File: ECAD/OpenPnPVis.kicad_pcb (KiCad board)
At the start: 4 copper layers, 40 x 47.4 mm, 73 parts, among them J1 USB3_B, J2 Conn_01x02, J3 Conn_01x02, Q1 CJ2305, U1 AMS1117-3.3, U10 AP2127K-2.5, U2 ﻿AR0144, U3 FT602Q, U4 AP2127K-2.8, U5 TPD4EUSB30, U6 AP2127K-1.2, U7 ATtiny10-TS, U8 74LVC2G74, U9 TPD2EUSB30, Y1 30MHz

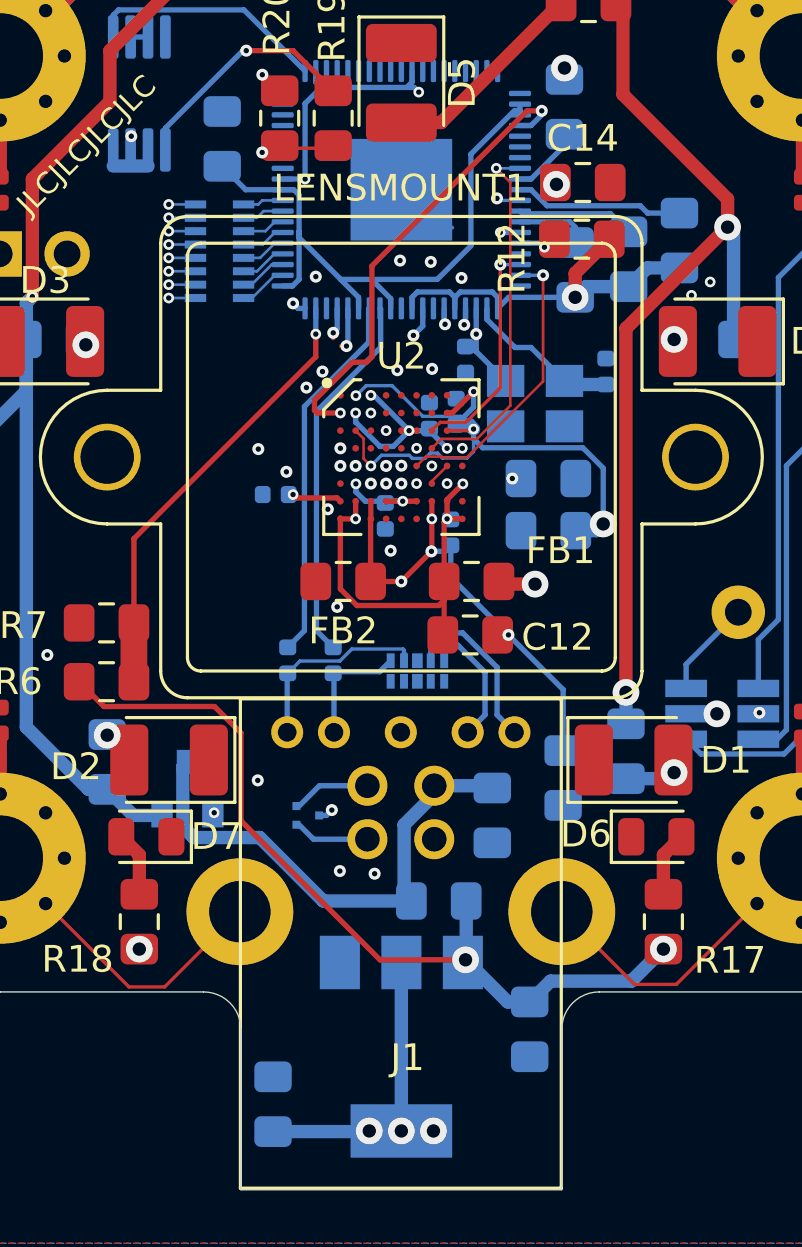
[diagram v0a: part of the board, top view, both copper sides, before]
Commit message: Added Courtyard to Lens mount
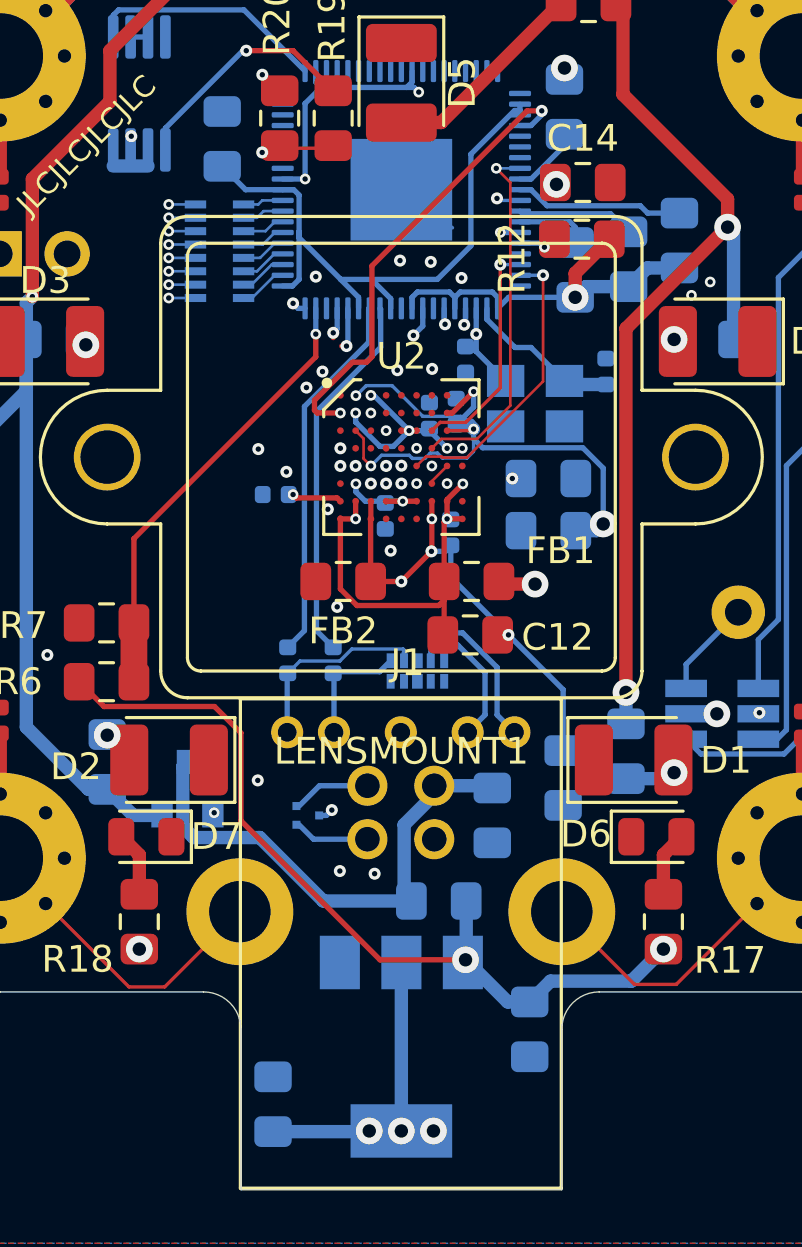
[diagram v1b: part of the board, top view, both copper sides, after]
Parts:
- J1: footprint Image_Sensors:U235-091N-4BLRC16-4-5 -> OpenPnPVis:U235-091N-4BLRC16-4-5
- LENSMOUNT1: footprint Image_Sensors:CMT168-1122F -> OpenPnPVis:CMT168-1122F
- U2: footprint Image_Sensors:BGA-72_9x8_5.565x5.545mm -> OpenPnPVis:BGA-72_9x8_5.565x5.545mm
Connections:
- U3 pad 77: GND -> (no net)

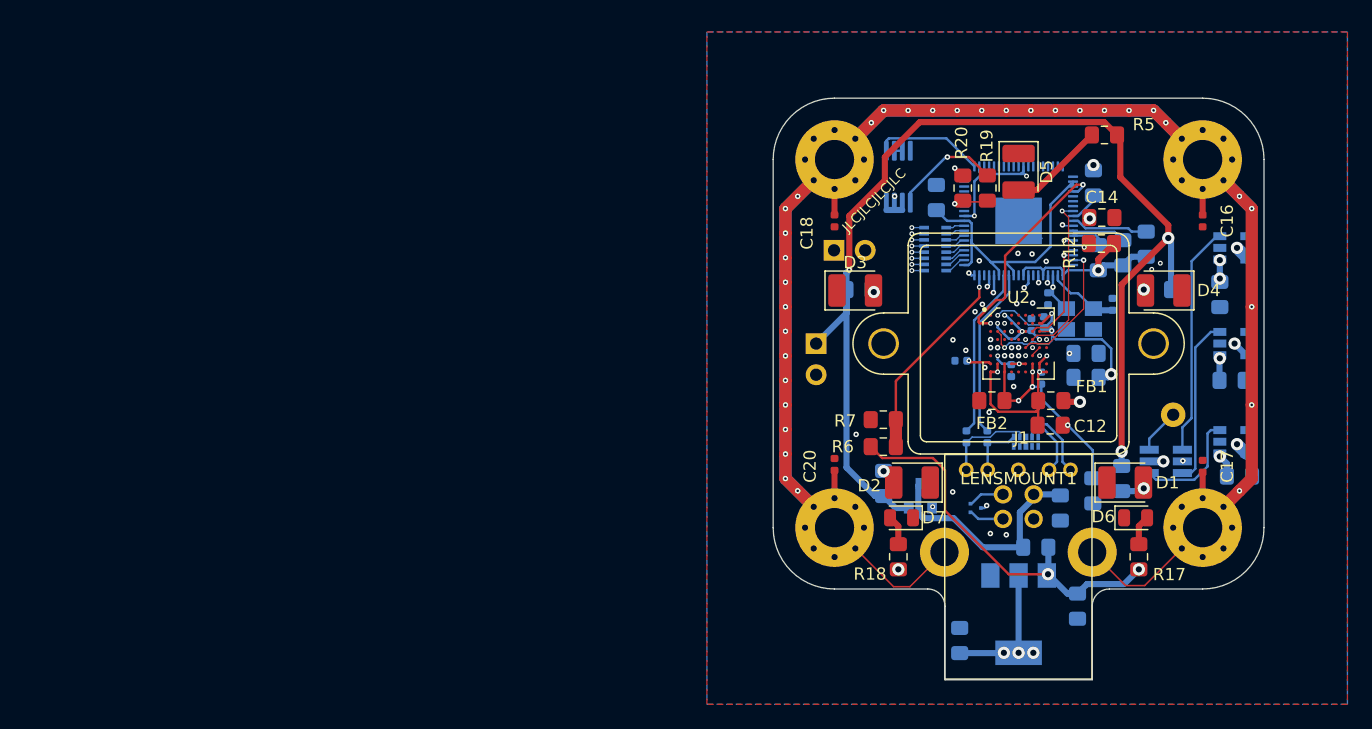
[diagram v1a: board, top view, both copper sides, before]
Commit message: Creation of Rev003
Creation of Rev003. This is a mini-sized board for easier fitment into tight spaces. The USB connector has changed to a USB Type-C. Some components have changed footprint to 0402.
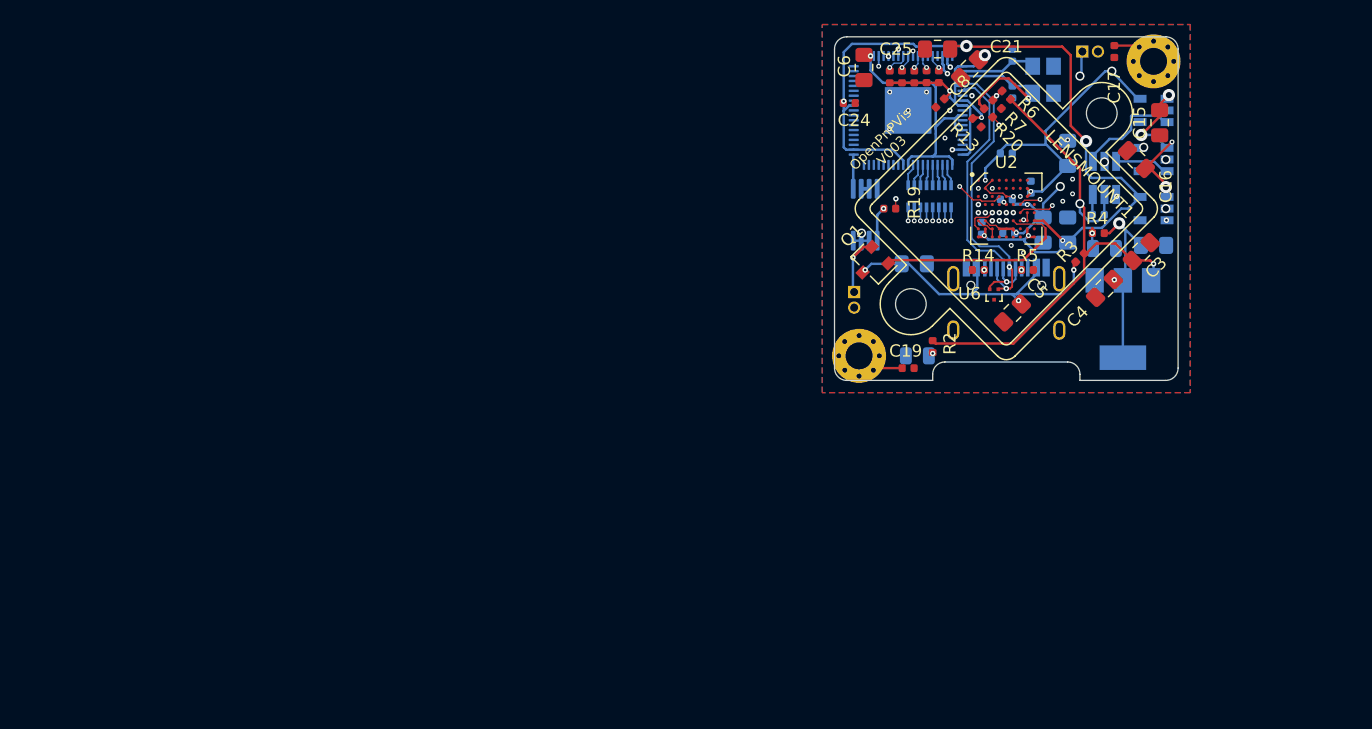
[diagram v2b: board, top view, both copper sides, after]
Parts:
- removed C20: 100nF, Capacitor_SMD:C_0402_1005Metric
- removed D3, D4, D5: LED, LED_SMD:LED_1210_3225Metric_Pad1.42x2.65mm_HandSolder
- removed D6, D7: LED, LED_SMD:LED_0805_2012Metric
- removed FB1, FB2: Ferrite_Bead_Small, Resistor_SMD:R_0805_2012Metric_Pad1.15x1.40mm_HandSolder
- removed H3, H4: M3, MountingHole:MountingHole_3.2mm_M3_Pad_Via
- removed J1: USB3_B, OpenPnPVis:U235-091N-4BLRC16-4-5
- removed R16: 0R, Resistor_SMD:R_0805_2012Metric_Pad1.15x1.40mm_HandSolder
- removed R17, R18: 100, Resistor_SMD:R_0805_2012Metric_Pad1.15x1.40mm_HandSolder
- removed TP1: TestPoint, TestPoint:TestPoint_Loop_D1.80mm_Drill1.0mm_Beaded
- removed U5: TPD4EUSB30, Package_SON:USON-10_2.5x1.0mm_P0.5mm
- added C24: 100nF, Capacitor_SMD:C_0402_1005Metric, F.Cu at (141.2, 85.4)
- added C25: 10uF, Capacitor_SMD:C_0805_2012Metric_Pad1.15x1.40mm_HandSolder, F.Cu at (148.4, 81.0)
- added J4: USB_C_Receptacle, Type-C:HRO-TYPE-C-31-M-12-Assembly, B.Cu at (154.0, 106.5)
- C1, C2: value 100nF -> 16pF
- C12, C14: moved to B.Cu
- C15, C21, C5: moved to F.Cu
- C16: value 100nF -> 10uF; footprint Capacitor_SMD:C_0402_1005Metric -> Capacitor_SMD:C_0805_2012Metric_Pad1.15x1.40mm_HandSolder
- C18: value 100nF -> 10uF; footprint Capacitor_SMD:C_0402_1005Metric -> Capacitor_SMD:C_0805_2012Metric_Pad1.15x1.40mm_HandSolder; moved to B.Cu
- C19, C8: value 10uF -> 100nF; footprint Capacitor_SMD:C_0805_2012Metric_Pad1.15x1.40mm_HandSolder -> Capacitor_SMD:C_0402_1005Metric; moved to F.Cu
- C3, C4: value 100nF -> 10uF; footprint Capacitor_SMD:C_0402_1005Metric -> Capacitor_SMD:C_0805_2012Metric_Pad1.15x1.40mm_HandSolder; moved to F.Cu
- C6: value 4.7uF -> 10uF; moved to F.Cu
- D1, D2: footprint LED_SMD:LED_1210_3225Metric_Pad1.42x2.65mm_HandSolder -> LED_SMD:LED_0805_2012Metric; moved to B.Cu
- H1, H2: footprint MountingHole:MountingHole_3.2mm_M3_Pad_Via -> MountingHole:MountingHole_2.2mm_M2_Pad_Via
- J2, J3: footprint Connector_PinHeader_2.54mm:PinHeader_1x02_P2.54mm_Vertical -> Connector_PinHeader_1.27mm:PinHeader_1x02_P1.27mm_Vertical
- Q1: value CJ2305 -> SMD-MOSFET-P-CH-8V-4.1A-CJ2305_SOT-23_; moved to F.Cu
- R1: value 100 -> 10K; footprint Resistor_SMD:R_0805_2012Metric_Pad1.15x1.40mm_HandSolder -> Resistor_SMD:R_0402_1005Metric
- R10, R11, R13, R8, R9: footprint Resistor_SMD:R_0805_2012Metric_Pad1.15x1.40mm_HandSolder -> Resistor_SMD:R_0402_1005Metric; moved to F.Cu
- R12, R19, R20, R6, R7: footprint Resistor_SMD:R_0805_2012Metric_Pad1.15x1.40mm_HandSolder -> Resistor_SMD:R_0402_1005Metric
- R14: value 0R -> 5.1K; footprint Resistor_SMD:R_0805_2012Metric_Pad1.15x1.40mm_HandSolder -> Resistor_SMD:R_0402_1005Metric; moved to F.Cu
- R2: value 100 -> 85; footprint Resistor_SMD:R_0805_2012Metric_Pad1.15x1.40mm_HandSolder -> Resistor_SMD:R_0402_1005Metric; moved to F.Cu
- R3, R4: value 100 -> 0R; footprint Resistor_SMD:R_0805_2012Metric_Pad1.15x1.40mm_HandSolder -> Resistor_SMD:R_0402_1005Metric; moved to F.Cu
- R5: value 100 -> 5.1K; footprint Resistor_SMD:R_0805_2012Metric_Pad1.15x1.40mm_HandSolder -> Resistor_SMD:R_0402_1005Metric
- U4: value AP2127K-2.8 -> ATtiny10-TS; footprint Package_TO_SOT_SMD:SOT-23-5 -> Package_TO_SOT_SMD:SOT-23-6_Handsoldering
- U6: value AP2127K-1.2 -> TPD2EUSB30; footprint Package_TO_SOT_SMD:SOT-23-5 -> Package_TO_SOT_SMD:Texas_DRT-3; moved to F.Cu
- U7: value ATtiny10-TS -> AP2127K-2.8; footprint Package_TO_SOT_SMD:SOT-23-6_Handsoldering -> Package_TO_SOT_SMD:SOT-23-5
- U9: value TPD2EUSB30 -> AP2127K-1.2; footprint Package_TO_SOT_SMD:Texas_DRT-3 -> Package_TO_SOT_SMD:SOT-23-5
- Y1: value 30MHz -> X3S030000BA1H-U
- moved H1 46.0 mm to (166.0, 82.0)
- moved C8 43.8 mm to (148.6, 85.4), turned to 225 degrees
- moved C17 34.6 mm to (162.8, 81.2), turned to 90 degrees
- moved C21 33.2 mm to (151.0, 82.6), turned to 225 degrees
- moved U9 31.9 mm to (166.0, 90.0), turned to 180 degrees
- moved H2 31.3 mm to (142.0, 106.0)
- moved C7 30.9 mm to (146.5, 98.5), turned to 180 degrees
- moved R6 30.4 mm to (154.0, 84.8), turned to 135 degrees
- moved U7 28.6 mm to (166.0, 86.0)
- moved C19 28.4 mm to (146.0, 107.0)
- moved R7 27.3 mm to (153.2, 85.5), turned to 135 degrees
- moved C18 26.1 mm to (166.0, 97.0), turned to 180 degrees
- moved J3 25.9 mm to (160.2, 81.2)
- moved U1 25.5 mm to (163.5, 103.0)
- moved D2 24.7 mm to (162.0, 97.2)
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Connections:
- net /FLASH_SIG renamed FLASH_SIG
- C11 pad 1: /VAA -> VAA
- C11 pad 2: GNDA -> GND
- C12 pad 1: /VAA -> VAA
- C12 pad 2: GNDA -> GND
- C16 pad 2: Earth -> +3V3
- C17 pad 2: Earth -> Net-(C17-Pad2)
- C18 pad 2: Earth -> +3V3
- C19 pad 2: +3V3 -> Net-(C19-Pad2)
- C21 pad 1: GND -> +3V3
- C21 pad 2: +3V3 -> GND
- C3 pad 1: /USB_SSTX-_C -> +5V
- C3 pad 2: /USB_SSTX- -> GND
- C4 pad 1: /USB_SSTX+_C -> +3V3
- C4 pad 2: /USB_SSTX+ -> GND
- C5 pad 1: /VIN -> /Power/VIN
- C7 pad 1: +5V -> GND
- C7 pad 2: GND -> /Power/VIN
- H1 pad 1: Earth -> Net-(C17-Pad2)
- H2 pad 1: Earth -> Net-(C19-Pad2)
- J2 pad 1: /LED_V+ -> LED_V+
- Q1 pad 2: /LED_V+ -> LED_V+
- Q1 pad 3: /VIN -> /Power/VIN
- R1 pad 1: /LED_V+ -> /Power/AT_TINY_RST
- R1 pad 2: Net-(D1-Pad2) -> +5V
- R14 pad 1: GNDA -> GND
- R14 pad 2: GND -> Net-(J4-PadB5)
- R2 pad 1: /LED_V+ -> +5V
- R2 pad 2: Net-(D2-Pad2) -> Net-(D1-Pad2)
- R3 pad 1: /LED_V+ -> /Power/VIN
- R3 pad 2: Net-(D3-Pad2) -> +5V
- R4 pad 1: /LED_V+ -> +3V3
- R4 pad 2: Net-(D4-Pad2) -> Net-(D2-Pad2)
- R5 pad 1: /LED_V+ -> Net-(J4-PadA5)
- R5 pad 2: Net-(D5-Pad2) -> GND
- U10 pad 3: /2V5_EN -> /Power/2V5_EN
- U10 pad 5: +2V5 -> VAA
- U2 pad D9: GNDA -> GND
- U2 pad F9: /VAA -> VAA
- U2 pad G2: /VAA -> VAA
- U2 pad G3: GNDA -> GND
- U2 pad G7: GNDA -> GND
- U2 pad G8: /VAA -> VAA
- U2 pad H1: /VAA -> VAA
- U2 pad H2: /VAA -> VAA
- U2 pad H3: GNDA -> GND
- U2 pad H7: GNDA -> GND
- U2 pad H8: /VAA -> VAA
- U2 pad H9: /VAA -> VAA
- U3 pad 14: +2V5 -> VAA
- U3 pad 23: /USB_D+ -> USB_D+
- U3 pad 25: /USB_D- -> USB_D-
- U3 pad 31: /USB_SSTX+ -> Net-(U3-Pad31)
- U3 pad 32: /USB_SSTX- -> Net-(U3-Pad32)
- U3 pad 34: /USB_SSRX+ -> Net-(U3-Pad34)
- U3 pad 35: /USB_SSRX- -> Net-(U3-Pad35)
- U3 pad 49: +2V5 -> VAA
- U3 pad 59: +2V5 -> VAA
- U3 pad 68: +2V5 -> VAA
- U3 pad 77: (no net) -> GND
- U4 pad 1: +3V3 -> /Power/2V8_EN
- U4 pad 3: /2V8_EN -> /Power/1V2_EN
- U4 pad 4: Net-(U4-Pad4) -> /Power/2V5_EN
- U4 pad 5: +2V8 -> +5V
- U6 pad 1: +3V3 -> USB_D+
- U6 pad 2: GND -> USB_D-
- U6 pad 3: /1V2_EN -> GND
- U7 pad 1: /2V5_EN -> +3V3
- U7 pad 3: /1V2_EN -> /Power/2V8_EN
- U7 pad 4: /2V8_EN -> Net-(U7-Pad4)
- U7 pad 5: +5V -> +2V8
- U9 pad 1: /USB_D+ -> +3V3
- U9 pad 2: /USB_D- -> GND
- U9 pad 3: GND -> /Power/1V2_EN
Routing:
- net Earth: track 234.2 -> 0.00 mm, vias 33 -> 0
- net /LED_V+: track 93.5 -> 0.00 mm, vias 3 -> 0
- net VAA: track 0.00 -> 73.3 mm, vias 0 -> 6
- net +2V5: track 48.8 -> 0.00 mm, vias 5 -> 0
- net /USB_D+: track 28.5 -> 0.00 mm, vias 1 -> 0
- net /USB_SSRX+: track 28.1 -> 0.00 mm, vias 1 -> 0
- net /USB_D-: track 27.7 -> 0.00 mm, vias 1 -> 0
- net /Power/VIN: track 0.00 -> 26.4 mm, vias 0 -> 3
- net /USB_SSRX-: track 25.6 -> 0.00 mm, vias 1 -> 0
- net USB_D+: track 0.00 -> 24.7 mm, vias 0 -> 2
- net USB_D-: track 0.00 -> 24.1 mm, vias 0 -> 1
- net GNDA: track 21.6 -> 0.00 mm, vias 5 -> 0
- net /VIN: track 19.3 -> 0.00 mm
- net /2V5_EN: track 18.8 -> 0.00 mm
- net /VAA: track 15.3 -> 0.00 mm, vias 3 -> 0
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- added copper zone on In1.Cu, net GND
- added copper zone on In2.Cu, net GND
- removed copper zone on In2.Cu, net +1V2
- removed copper zone on In1.Cu, net +2V8
- removed copper zone on In1.Cu, net +3V3
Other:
- board size 40 x 47.4 mm -> 28 x 28 mm
- net class Clock added: clearance 0.1, trace_width 0.21, via_dia 0.45, via_drill 0.2
- net class Power added: clearance 0.1, trace_width 0.2, via_dia 0.45, via_drill 0.2
- net class USB Data added: clearance 0.1, trace_width 0.153, via_dia 0.45, via_drill 0.2
- net class Video Data added: clearance 0.1, trace_width 0.146, via_dia 0.4, via_drill 0.2
- net class Video Data_inner added: clearance 0.1, trace_width 0.131, via_dia 0.4, via_drill 0.2
- board text added: "Impedances Calculated for JLC 2313"
- board text added: "OpenPnPVis V003"
- board text added: "TRIG"
- board text removed: "JLCJLCJLCJLC"
- board text removed: "LED GND"
- board text removed: "LED V+"
- board text removed: "OpenPnPVis V002 DEC 2020"

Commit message: V004 Update
Added ICSP pads
Updated 74LVC2G74 footprint
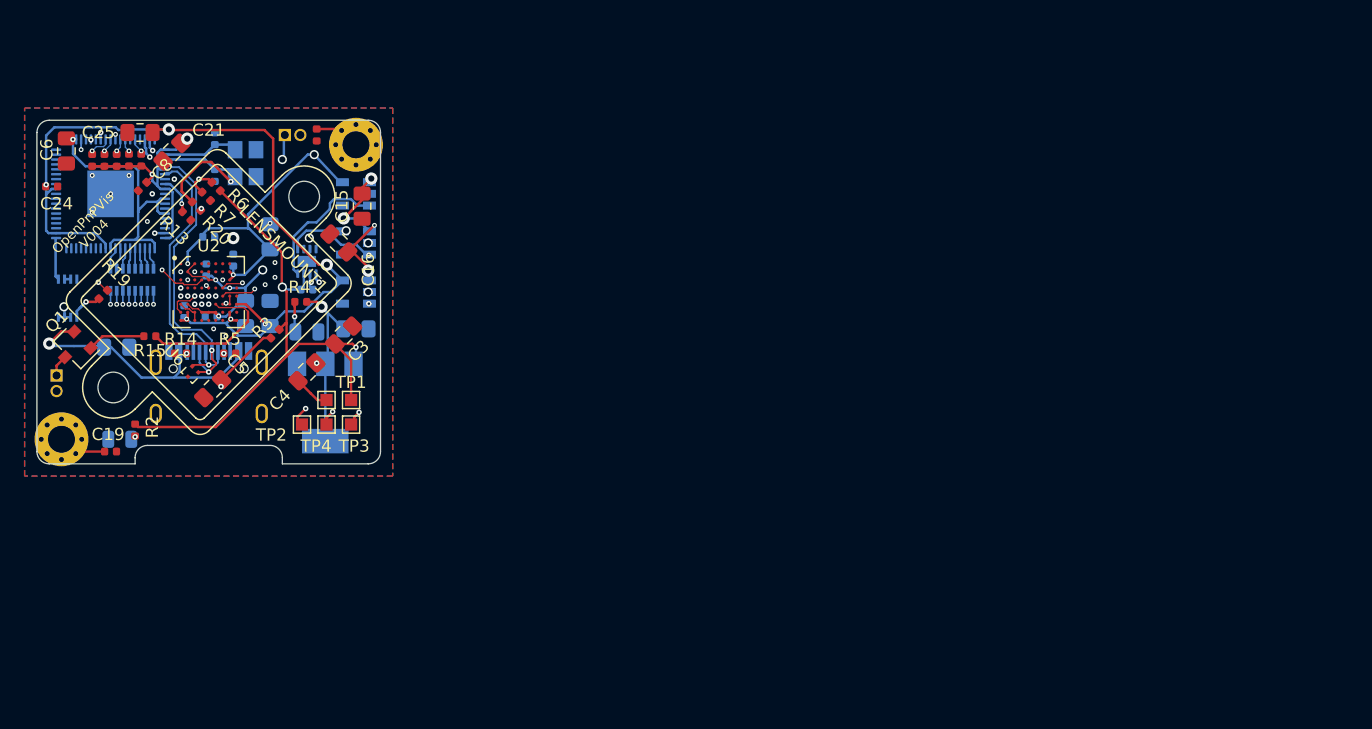
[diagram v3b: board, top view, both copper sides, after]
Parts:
- added R15: 1.6K, Resistor_SMD:R_0402_1005Metric, F.Cu at (84.2, 104.4)
- added TP1: TestPoint, TestPoint:TestPoint_Pad_1.0x1.0mm, F.Cu at (100.6, 109.6)
- added TP2: TestPoint, TestPoint:TestPoint_Pad_1.0x1.0mm, F.Cu at (96.6, 111.6)
- added TP3: TestPoint, TestPoint:TestPoint_Pad_1.0x1.0mm, F.Cu at (100.6, 111.6)
- added TP4: TestPoint, TestPoint:TestPoint_Pad_1.0x1.0mm, F.Cu at (98.6, 111.6)
- added TP5: TestPoint, TestPoint:TestPoint_Pad_1.0x1.0mm, F.Cu at (98.6, 109.6)
- Q1: value SMD-MOSFET-P-CH-8V-4.1A-CJ2305_SOT-23_ -> SMD-MOSFET-N-CH-20V-2.1A-CJ2302_SOT-23_
- U4: value ATtiny10-TS -> ATTINY10-MAHR; footprint Package_TO_SOT_SMD:SOT-23-6_Handsoldering -> Package_DFN_QFN:DFN-8-1EP_2x2mm_P0.5mm_EP0.9x1.5mm
- U8: footprint Package_SO:MSOP-8_3x3mm_P0.65mm -> Package_SO:VSSOP-8_2.4x2.1mm_P0.5mm
- moved R3 65.9 mm to (94.4, 104.2)
- moved U6 65.7 mm to (87.6, 107.4), turned to 135 degrees
- moved C5 65.5 mm to (89.3, 108.7)
- moved C22 65.5 mm to (88.8, 99.0), turned to 90 degrees
- moved Q1 65.4 mm to (78.0, 105.4)
- moved C17 65.4 mm to (97.8, 88.0)
- moved C1 65.4 mm to (89.5, 88.3)
- moved C10 65.4 mm to (94.0, 96.3)
- moved C11 65.4 mm to (87.0, 102.4)
- moved C12 65.4 mm to (94.0, 102.5)
- moved C14 65.4 mm to (92.0, 102.5)
- moved C15 65.4 mm to (101.5, 93.8)
- moved C16 65.4 mm to (99.6, 96.8)
- moved C18 65.4 mm to (101.0, 103.8)
- moved C19 65.4 mm to (81.0, 113.8)
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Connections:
- Q1 pad 1: FLASH_SIG -> Net-(Q1-Pad1)
- Q1 pad 2: LED_V+ -> /Power/VIN
- Q1 pad 3: /Power/VIN -> LED_V+
- U4 pad 1: /Power/2V8_EN -> /Power/1V2_EN
- U4 pad 2: GND -> Net-(U4-Pad2)
- U4 pad 3: /Power/1V2_EN -> Net-(U4-Pad3)
- U4 pad 4: /Power/2V5_EN -> GND
- U4 pad 5: +5V -> /Power/2V5_EN
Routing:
- net /Power/1V2_EN: track 4.48 -> 29.4 mm, vias 0 -> 2
- net /Power/AT_TINY_RST: track 1.66 -> 13.5 mm, vias 0 -> 2
- net /Power/2V5_EN: track 5.36 -> 16.2 mm, vias 2 -> 3
- net /C_DAT4: track 20.3 -> 12.6 mm
- net FLASH_SIG: track 17.4 -> 12.2 mm
- net Net-(Q1-Pad1): track 0.00 -> 4.74 mm
- net GND: track 3.65 -> 6.62 mm, vias 19 -> 20
- net LED_V+: track 4.74 -> 1.92 mm, vias 1 -> 0
- net +5V: track 44.4 -> 47.1 mm
- net /Power/2V8_EN: track 8.73 -> 11.3 mm
- net /Power/VIN: track 26.4 -> 28.8 mm, vias 3 -> 2
- net +2V8: track 50.5 -> 52.1 mm
- net Net-(R6-Pad2): track 7.83 -> 9.15 mm
- net +1V2: track 26.0 -> 24.9 mm
- net VAA: track 73.3 -> 72.4 mm
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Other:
- board text added: "JLCJLCJLCJLC"
- board text added: "OpenPnPVis V004"
- board text removed: "OpenPnPVis V003"
